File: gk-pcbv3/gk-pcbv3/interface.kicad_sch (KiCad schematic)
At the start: 82 parts, among them J11 Conn_01x02, J13 Conn_01x02, J7 Conn_01x02, Q1 MMBT3904, Q2 MMBT3904, SW3 RotaryEncoder_Switch, SW4 SW_DIP_x01, U9 LSM6DSL

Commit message: v3 board
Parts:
- removed C60: 10n, Capacitor_SMD:C_0603_1608Metric, symbol Device:C
- removed C61: 10u, Capacitor_SMD:C_0805_2012Metric, symbol Device:C
- removed C62: 100n, Capacitor_SMD:C_0603_1608Metric, symbol Device:C
- removed J7: Conn_01x02, Connector_PinHeader_2.54mm:PinHeader_1x02_P2.54mm_Vertical, symbol Connector_Generic:Conn_01x02
- removed MOD1: ATWINC1500-MR210PB, digikey:WIFI_Module_ATWINC1500-MR210PB, symbol ATWINC1500:ATWINC1500-MR210PB
- removed R25: 1M, Resistor_SMD:R_0603_1608Metric, symbol Device:R
- removed R26, R27: 100k, Resistor_SMD:R_0603_1608Metric, symbol Device:R
- removed R82, R84, R86: NC, Resistor_SMD:R_0603_1608Metric, symbol Device:R
- removed R83, R85, R87: 0R, Resistor_SMD:R_0603_1608Metric, symbol Device:R
- removed SW3: RotaryEncoder_Switch, Rotary_Encoder:RotaryEncoder_Alps_EC11E-Switch_Vertical_H20mm, symbol Device:RotaryEncoder_Switch
- removed SW4: SW_DIP_x01, Button_Switch_THT:SW_DIP_SPSTx01_Slide_9.78x4.72mm_W7.62mm_P2.54mm, symbol Switch:SW_DIP_x01
- added J15: Conn_01x02, Connector_PinHeader_2.54mm:PinHeader_1x02_P2.54mm_Vertical, symbol Connector_Generic:Conn_01x02
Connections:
- net JR_5 is gone; now on net GND: SW2.5
- net JR_6 is gone; now on net JOY_X: SW2.6
- net JR_7 is gone; now on net VCC: SW2.7
- net VREGEN: now also J15.2 (Pin_2)
- net VREGIN: now also J15.1 (Pin_1)
- net I2C4_SCL renamed I2C2_SCL
- net I2C4_SDA renamed I2C2_SDA
- no-connect marks 8 -> 1
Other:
- note added: "ON/OFF triggers an NPN to enable VREG as well as trigger a GPIO The MCU also needs to be able to trigger the VREG Finally, we provide a jumper for debugging purposes to keep the system always on"
- note removed: "ON/OFF triggers an NPN to enable VREG as well as trigger a GPIO The MCU also needs to be able to trigger the VREG Finally, we provide a slide switch for debugging purposes to keep the system always on"
- note removed: "Option to select rotary encoder (left) or joystick (right)"
- moved on the sheet: J11, R57

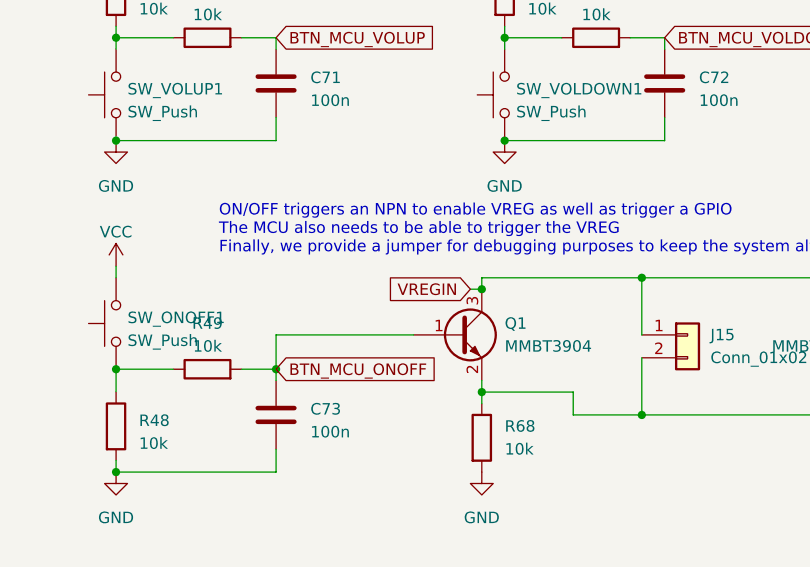
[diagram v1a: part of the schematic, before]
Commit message: redesign for better signal integrity
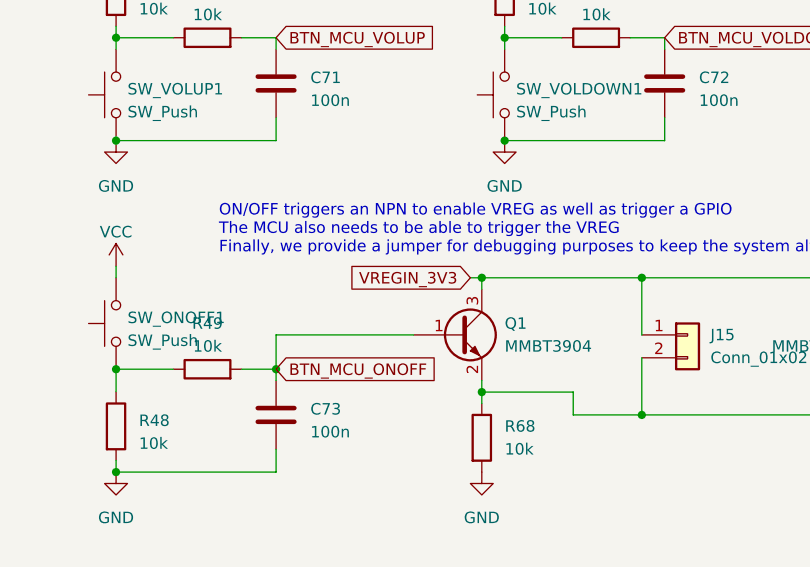
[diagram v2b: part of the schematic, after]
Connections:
- net VREGIN renamed VREGIN_3V3
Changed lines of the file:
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@@
-	)
-	(junction
-		(at 170.18 143.51)
-		(diameter 0)
-		(color 0 0 0 0)
 	)
 	(junction
@@
 	(junction
 		(at 73.66 24.13)
+		(diameter 0)
+		(color 0 0 0 0)
+	)
+	(junction
+		(at 170.18 142.24)
 		(diameter 0)
 		(color 0 0 0 0)
@@
 	(wire
 		(pts
+			(xy 170.18 142.24) (xy 170.18 143.51)
+		)
+		(stroke
+			(width 0)
+			(type default)
+		)
+	)
+	(wire
+		(pts
 			(xy 33.02 53.34) (xy 33.02 59.69)
 		)
@@
 	(wire
 		(pts
-			(xy 170.18 143.51) (xy 170.18 142.24)
-		)
-		(stroke
-			(width 0)
-			(type default)
-		)
-	)
-	(wire
-		(pts
 			(xy 232.41 114.3) (xy 232.41 115.57)
 		)
@@
 	(wire
 		(pts
-			(xy 168.91 143.51) (xy 170.18 143.51)
+			(xy 168.91 142.24) (xy 170.18 142.24)
 		)
 		(stroke
@@
 		)
 	)
-	(global_label "VREGIN"
+	(global_label "VREGIN_3V3"
 		(shape input)
-		(at 168.91 143.51 180)
+		(at 168.91 142.24 180)
 		(fields_autoplaced yes)
 		(effects
@@
 		)
 		(property "Intersheetrefs" "${INTERSHEET_REFS}"
-			(at 159.2119 143.51 0)
+			(at 154.7367 142.24 0)
 			(effects
 				(font

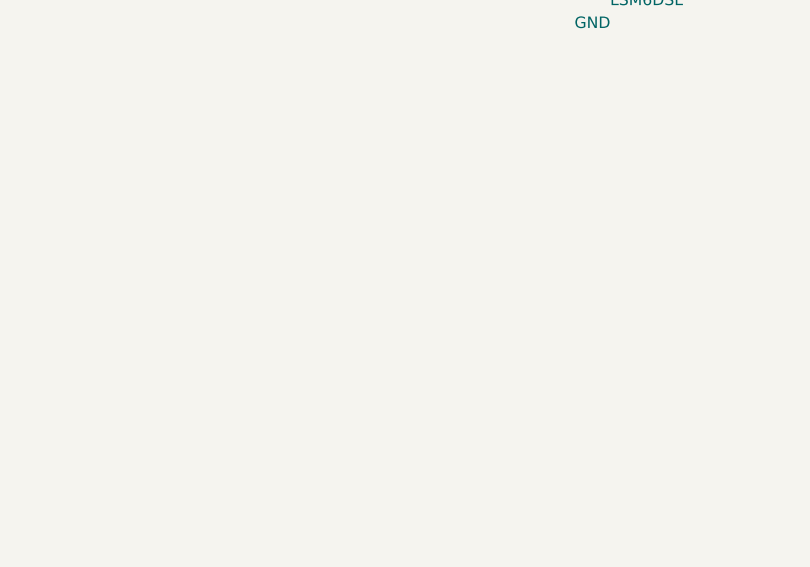
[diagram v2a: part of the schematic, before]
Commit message: begin wifi integration
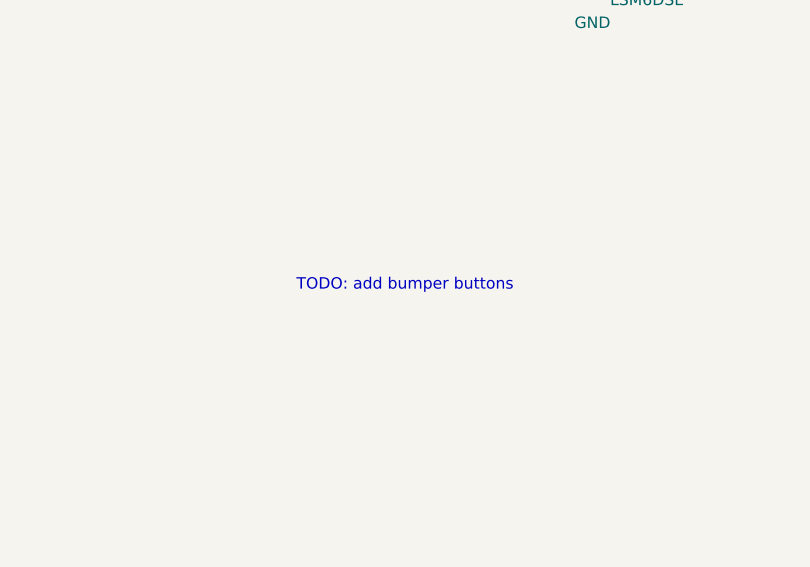
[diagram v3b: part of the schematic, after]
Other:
- note added: "TODO: add bumper buttons"
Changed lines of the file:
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@@
+		)
+	)
+	(text "TODO: add bumper buttons\n"
+		(exclude_from_sim no)
+		(at 60.452 128.27 0)
+		(effects
+			(font
+				(size 1.27 1.27)
+			)
 		)
 	)

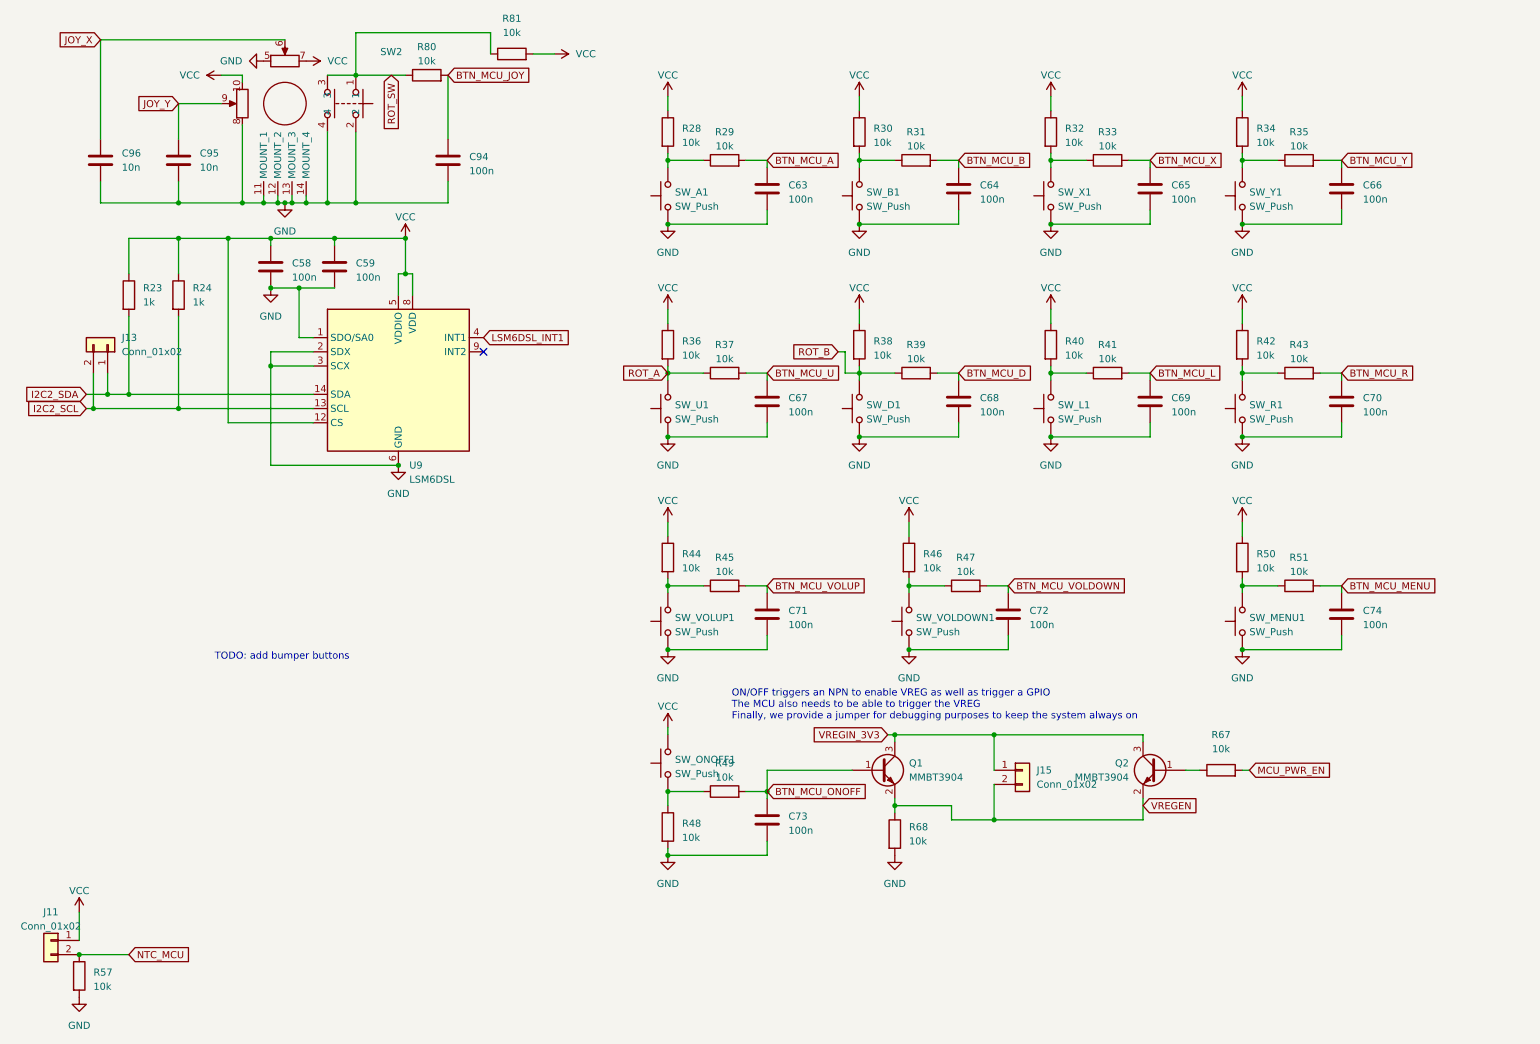
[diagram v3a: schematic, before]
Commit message: update schematics for new vreg design
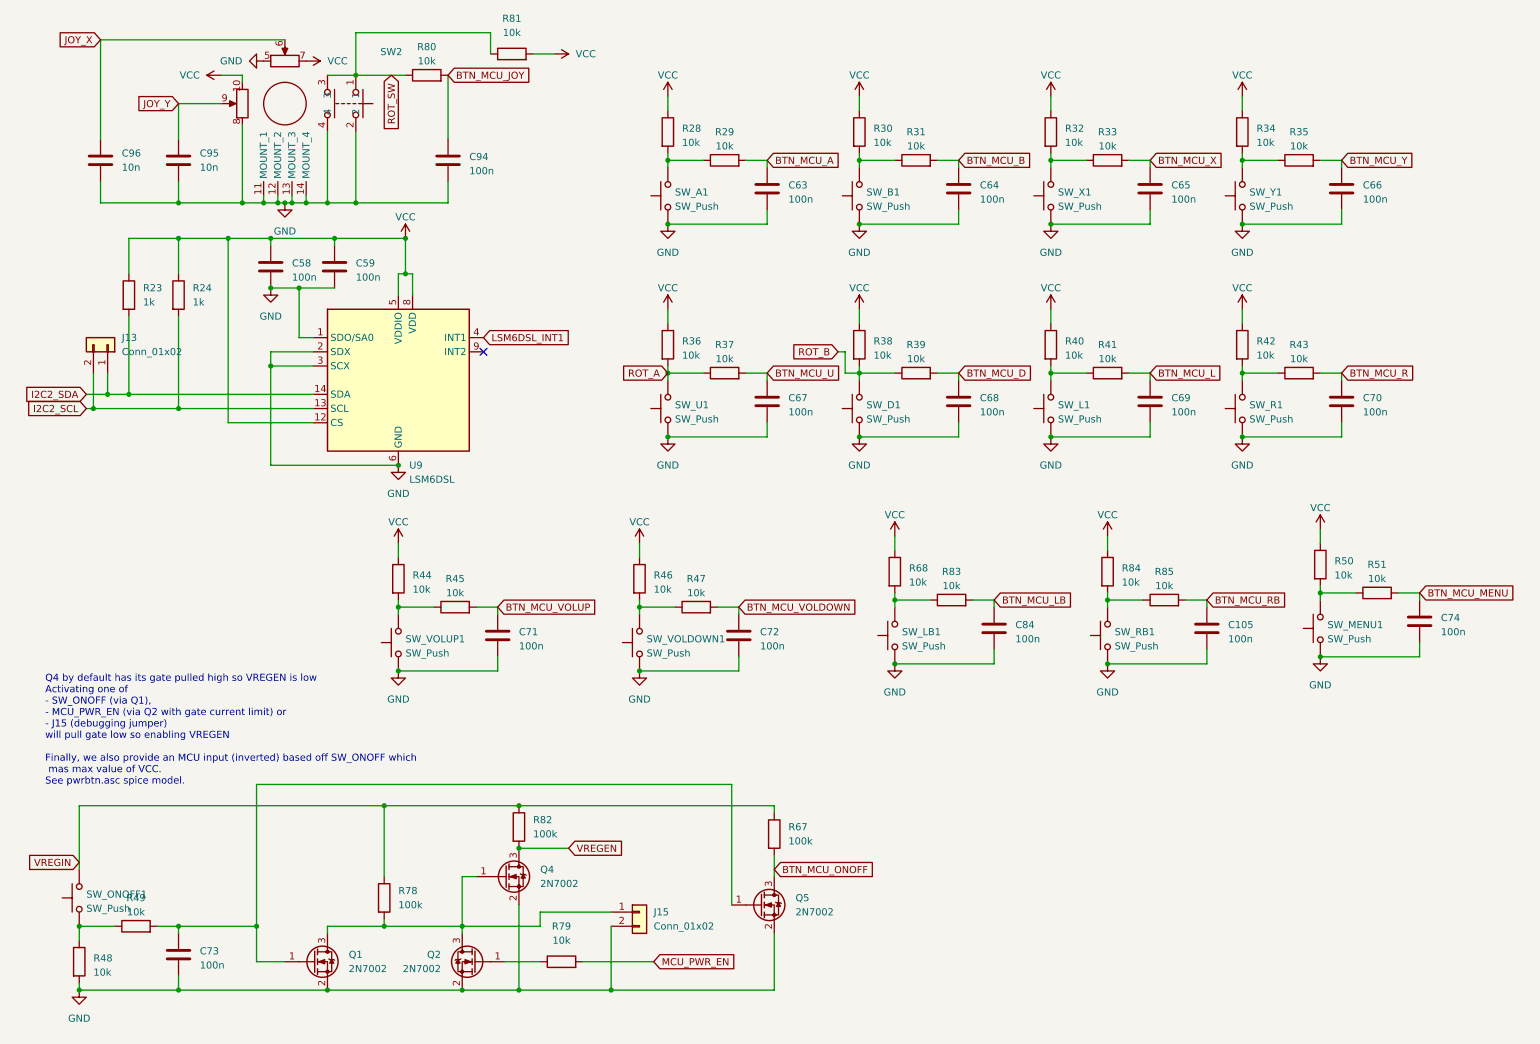
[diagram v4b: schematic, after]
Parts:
- removed J11: Conn_01x02, Connector_JST:JST_XH_S2B-XH-A_1x02_P2.50mm_Horizontal, symbol Connector_Generic:Conn_01x02
- removed Q1, Q2: MMBT3904, Package_TO_SOT_SMD:SOT-23, symbol Transistor_BJT:MMBT3904
- removed R57: 10k, Resistor_SMD:R_0603_1608Metric, symbol Device:R
- added C105, C84: 100n, Capacitor_SMD:C_0603_1608Metric, symbol Device:C
- added Q1, Q2, Q4, Q5: 2N7002, Package_TO_SOT_SMD:SOT-23, symbol Transistor_FET:2N7002
- added R78, R82: 100k, Resistor_SMD:R_0603_1608Metric, symbol Device:R
- added R79, R83, R84, R85: 10k, Resistor_SMD:R_0603_1608Metric, symbol Device:R
- added SW_LB1, SW_RB1: SW_Push, Button_Switch_THT:SW_Tactile_SKHH_Angled, symbol Switch:SW_Push
- R67: value 10k -> 100k
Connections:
- net BTN_MCU_ONOFF: now also R67.2, Q5.3 (D); no longer C73.1, R49.2
- net GND: now also J15.2 (Pin_2), C105.2, C84.2, Q1.2 (S), Q2.2 (S), Q4.2 (S), Q5.2 (S), SW_LB1.1, SW_RB1.1; no longer R68.2
- net MCU_PWR_EN: now also R79.2; no longer R67.2
- net VCC: now also R68.1, R84.1; no longer SW_ONOFF1.2
- net VREGEN: now also Q4.3 (D), R82.2; no longer J15.2 (Pin_2), R68.1
- net VREGIN: now reaches R67.1
- net VREGIN: now also SW_ONOFF1.2, R78.1, R82.1
- net VREGIN_3V3: no longer names the net of J15.1 (Pin_1)
- net VREGIN_3V3: now also Q1.3 (D), Q2.3 (D), Q4.1 (G), R78.2
- new net: Q2.1 (G), R79.1
- new net: C73.1, Q1.1 (G), Q5.1 (G), R49.2
- new net: R68.2, R83.1, SW_LB1.2
- new net: R84.2, R85.1, SW_RB1.2
- new net BTN_MCU_LB: C84.1, R83.2
- new net BTN_MCU_RB: C105.1, R85.2
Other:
- note added: "Q4 by default has its gate pulled high so VREGEN is low Activating one of - SW_ONOFF (via Q1), - MCU_PWR_EN (via Q2 with gate current limit) or - J15 (debugging jumper) will pull gate low so enabling VREGEN Finally, we also provide an MCU input (inverted) based off SW_ONOFF which mas max value of VCC. See pwrbtn.asc spice model."
- note removed: "ON/OFF triggers an NPN to enable VREG as well as trigger a GPIO The MCU also needs to be able to trigger the VREG Finally, we provide a jumper for debugging purposes to keep the system always on"
- note removed: "TODO: add bumper buttons"
- moved on the sheet: C71, C72, C73, C74, J15, R44, R45, R46, R47, R48, R49, R50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

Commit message: new gerbers
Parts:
- SW_LB1, SW_RB1: footprint Button_Switch_THT:SW_Tactile_SKHH_Angled -> TerminalBlock:TerminalBlock_bornier-3_P5.08mm
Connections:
- net VCC: now also R67.1
- net VREGIN: no longer R67.1
- net LSM6DSL_INT1: no longer names the net of U9.4 (INT1)
- no-connect marks 1 -> 2
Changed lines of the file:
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@@
 	)
 	(junction
-		(at 102.87 154.94)
-		(diameter 0)
-		(color 0 0 0 0)
-	)
-	(junction
 		(at 92.71 187.96)
 		(diameter 0)
@@
 		(at 96.52 73.66)
 	)
+	(no_connect
+		(at 96.52 71.12)
+	)
 	(wire
 		(pts
@@
 	(wire
 		(pts
-			(xy 102.87 154.94) (xy 148.59 154.94)
-		)
-		(stroke
-			(width 0)
-			(type default)
-		)
-	)
-	(wire
-		(pts
 			(xy 55.88 176.53) (xy 55.88 182.88)
 		)
@@
 		)
 	)
-	(global_label "LSM6DSL_INT1"
-		(shape input)
-		(at 96.52 71.12 0)
-		(fields_autoplaced yes)
-		(effects
-			(font
-				(size 1.27 1.27)
-			)
-			(justify left)
-		)
-		(property "Intersheetrefs" "${INTERSHEET_REFS}"
-			(at 112.9119 71.12 0)
-			(effects
-				(font
-					(size 1.27 1.27)
-				)
-				(justify left)
-				(hide yes)
-			)
-		)
-	)
 	(global_label "MCU_PWR_EN"
 		(shape input)
@@
 		(fields_autoplaced yes)
 		(property "Reference" "SW_LB1"
-			(at 171.45 123.825 90)
+			(at 171.45 123.1899 90)
 			(effects
 				(font
@@
 		)
 		(property "Value" "SW_Push"
-			(at 171.45 126.365 90)
+			(at 171.45 125.7299 90)
 			(effects
 				(font
@@
 			)
 		)
-		(property "Footprint" "Button_Switch_THT:SW_Tactile_SKHH_Angled"
+		(property "Footprint" "TerminalBlock:TerminalBlock_bornier-3_P5.08mm"
 			(at 165.1 124.46 0)
 			(effects
@@
 	)
 	(symbol
+		(lib_name "VCC_1")
+		(lib_id "power:VCC")
+		(at 148.59 154.94 0)
+		(unit 1)
+		(exclude_from_sim no)
+		(in_bom yes)
+		(on_board yes)
+		(dnp no)
+		(fields_autoplaced yes)
+		(property "Reference" "#PWR0145"
+			(at 148.59 158.75 0)
+			(effects
+				(font
+					(size 1.27 1.27)
+				)
+				(hide yes)
+			)
+		)
+		(property "Value" "VCC"
+			(at 148.59 149.86 0)
+			(effects
+				(font
+					(size 1.27 1.27)
+				)
+			)
+		)
+		(property "Footprint" ""
+			(at 148.59 154.94 0)
+			(effects
+				(font
+					(size 1.27 1.27)
+				)
+				(hide yes)
+			)
+		)
+		(property "Datasheet" ""
+			(at 148.59 154.94 0)
+			(effects
+				(font
+					(size 1.27 1.27)
+				)
+				(hide yes)
+			)
+		)
+		(property "Description" "Power symbol creates a global label with name \"VCC\""
+			(at 148.59 154.94 0)
+			(effects
+				(font
+					(size 1.27 1.27)
+				)
+				(hide yes)
+			)
+		)
+		(pin "1"
+		)
+		(instances
+			(project ""
+				(path "/08730ac6-6084-459f-bdf1-86b322355ede/fa96f0b5-5dfb-45a6-bb43-c2cb84c619a5"
+					(reference "#PWR0145")
+					(unit 1)
+				)
+			)
+		)
+	)
+	(symbol
 		(lib_id "Transistor_FET:2N7002")
 		(at 100.33 167.64 0)
@@
 		(fields_autoplaced yes)
 		(property "Reference" "SW_RB1"
-			(at 209.55 123.825 90)
+			(at 209.55 123.1899 90)
 			(effects
 				(font
@@
 		)
 		(property "Value" "SW_Push"
-			(at 209.55 126.365 90)
+			(at 209.55 125.7299 90)
 			(effects
 				(font
@@
 			)
 		)
-		(property "Footprint" "Button_Switch_THT:SW_Tactile_SKHH_Angled"
+		(property "Footprint" "TerminalBlock:TerminalBlock_bornier-3_P5.08mm"
 			(at 203.2 124.46 0)
 			(effects
